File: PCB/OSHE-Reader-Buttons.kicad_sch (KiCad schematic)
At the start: 10 parts, among them SW1 SW_Push, SW2 SW_Push, SW3 SW_Push, SW4 SW_Push, SW5 SW_Push

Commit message: Footprint assignments
Added more footprints
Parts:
- R14, R15, R16, R17, R18: footprint (none) -> Resistor_SMD:R_1206_3216Metric
- SW1, SW2, SW3, SW4, SW5: footprint (none) -> Button_Switch_SMD:SW_Tactile_SPST_NO_Straight_CK_PTS636Sx25SMTRLFS
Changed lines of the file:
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@@
 			)
 		)
-		(property "Footprint" ""
+		(property "Footprint" "Button_Switch_SMD:SW_Tactile_SPST_NO_Straight_CK_PTS636Sx25SMTRLFS"
 			(at 105.41 88.9 0)
 			(effects
@@
 			)
 		)
-		(property "Footprint" ""
+		(property "Footprint" "Button_Switch_SMD:SW_Tactile_SPST_NO_Straight_CK_PTS636Sx25SMTRLFS"
 			(at 54.61 41.91 0)
 			(effects
@@
 			)
 		)
-		(property "Footprint" ""
+		(property "Footprint" "Resistor_SMD:R_1206_3216Metric"
 			(at 111.252 101.6 90)
 			(effects
@@
 			)
 		)
-		(property "Footprint" ""
+		(property "Footprint" "Resistor_SMD:R_1206_3216Metric"
 			(at 137.922 81.28 90)
 			(effects
@@
 			)
 		)
-		(property "Footprint" ""
+		(property "Footprint" "Button_Switch_SMD:SW_Tactile_SPST_NO_Straight_CK_PTS636Sx25SMTRLFS"
 			(at 129.54 68.58 0)
 			(effects
@@
 			)
 		)
-		(property "Footprint" ""
+		(property "Footprint" "Resistor_SMD:R_1206_3216Metric"
 			(at 64.262 82.55 90)
 			(effects
@@
 			)
 		)
-		(property "Footprint" ""
+		(property "Footprint" "Resistor_SMD:R_1206_3216Metric"
 			(at 64.262 52.07 90)
 			(effects
@@
 			)
 		)
-		(property "Footprint" ""
+		(property "Footprint" "Button_Switch_SMD:SW_Tactile_SPST_NO_Straight_CK_PTS636Sx25SMTRLFS"
 			(at 54.61 68.58 0)
 			(effects
@@
 			)
 		)
-		(property "Footprint" ""
+		(property "Footprint" "Button_Switch_SMD:SW_Tactile_SPST_NO_Straight_CK_PTS636Sx25SMTRLFS"
 			(at 128.27 44.45 0)
 			(effects
@@
 			)
 		)
-		(property "Footprint" ""
+		(property "Footprint" "Resistor_SMD:R_1206_3216Metric"
 			(at 139.192 55.88 90)
 			(effects

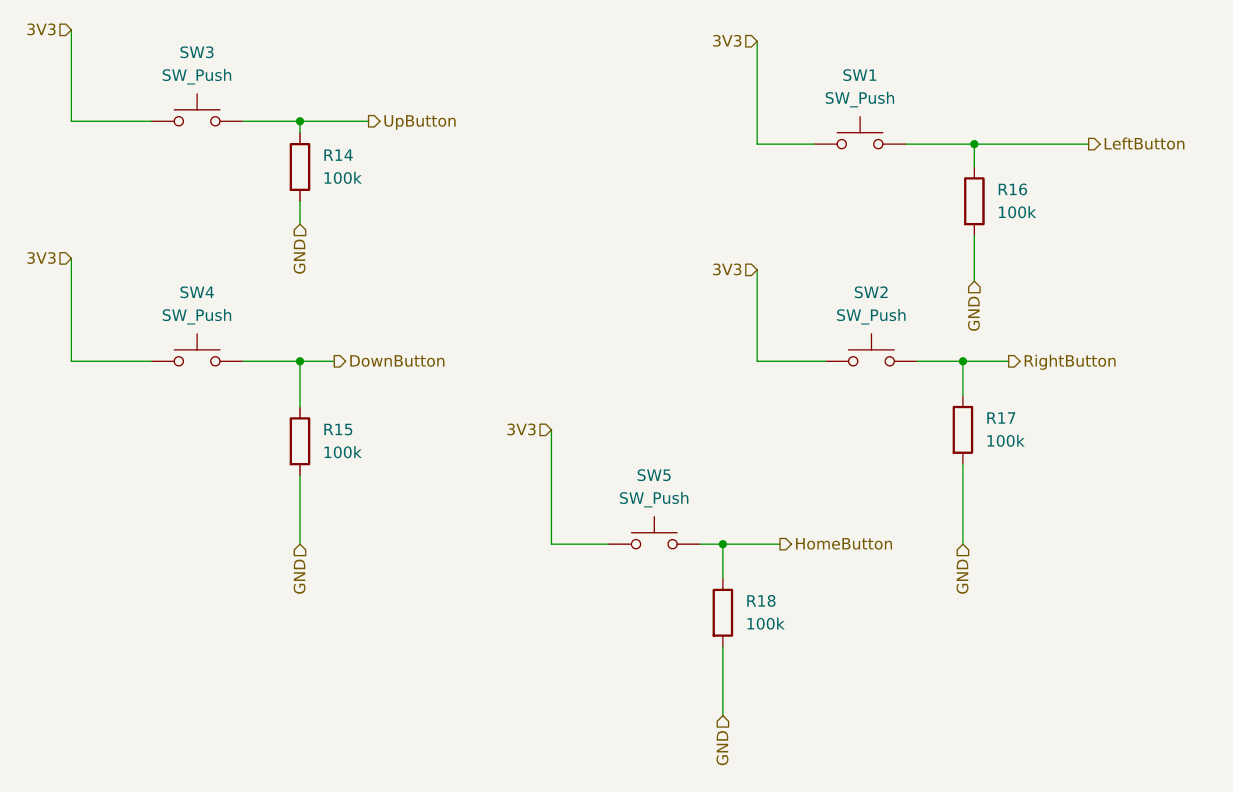
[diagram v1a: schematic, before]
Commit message: Footprints added
All footprints added (problem with J1 for some reason) ((pads of the display driver))
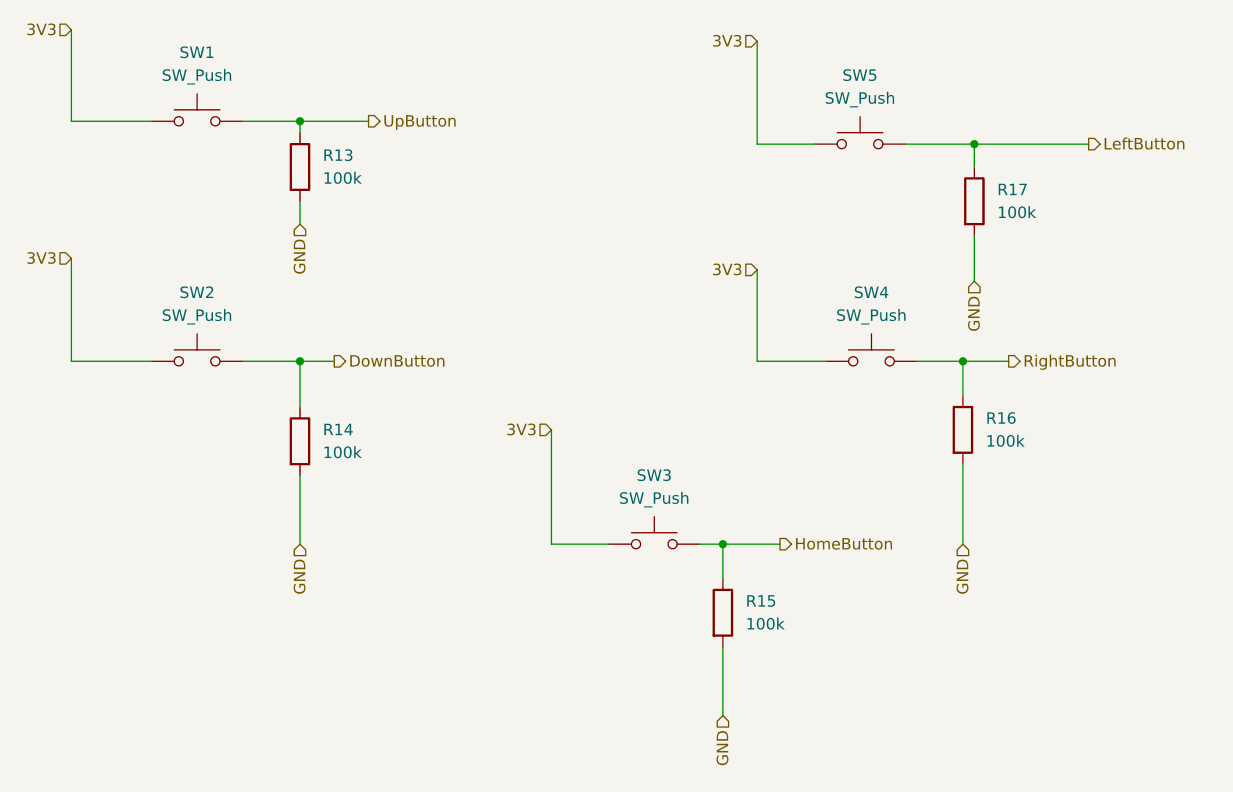
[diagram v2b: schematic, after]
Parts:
- renumbered R14 to R13, R15 to R14, R18 to R15, R17 to R16, R16 to R17, SW3 to SW1, SW4 to SW2, SW5 to SW3, SW2 to SW4, SW1 to SW5
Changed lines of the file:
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@@
 		(dnp no)
 		(fields_autoplaced yes)
-		(property "Reference" "SW5"
+		(property "Reference" "SW3"
 			(at 105.41 86.36 0)
 			(effects
@@
 				)
 			)
+			(project "OSHE-Reader-Buttons"
+				(path "/6556eb4f-dcf8-4b99-98b6-5934a7ce5a03"
+					(reference "SW3")
+					(unit 1)
+				)
+			)
 		)
 	)
@@
 		(on_board yes)
 		(dnp no)
-		(property "Reference" "SW3"
+		(property "Reference" "SW1"
 			(at 54.61 39.37 0)
 			(effects
@@
 				)
 			)
+			(project "OSHE-Reader-Buttons"
+				(path "/6556eb4f-dcf8-4b99-98b6-5934a7ce5a03"
+					(reference "SW1")
+					(unit 1)
+				)
+			)
 		)
 	)
@@
 		(dnp no)
 		(fields_autoplaced yes)
-		(property "Reference" "R18"
+		(property "Reference" "R15"
 			(at 115.57 100.3299 0)
 			(effects
@@
 				)
 			)
+			(project "OSHE-Reader-Buttons"
+				(path "/6556eb4f-dcf8-4b99-98b6-5934a7ce5a03"
+					(reference "R15")
+					(unit 1)
+				)
+			)
 		)
 	)
@@
 		(dnp no)
 		(fields_autoplaced yes)
-		(property "Reference" "R17"
+		(property "Reference" "R16"
 			(at 142.24 80.0099 0)
 			(effects
@@
 				)
 			)
+			(project "OSHE-Reader-Buttons"
+				(path "/6556eb4f-dcf8-4b99-98b6-5934a7ce5a03"
+					(reference "R16")
+					(unit 1)
+				)
+			)
 		)
 	)
@@
 		(dnp no)
 		(fields_autoplaced yes)
-		(property "Reference" "SW2"
+		(property "Reference" "SW4"
 			(at 129.54 66.04 0)
 			(effects
@@
 				)
 			)
+			(project "OSHE-Reader-Buttons"
+				(path "/6556eb4f-dcf8-4b99-98b6-5934a7ce5a03"
+					(reference "SW4")
+					(unit 1)
+				)
+			)
 		)
 	)
@@
 		(dnp no)
 		(fields_autoplaced yes)
-		(property "Reference" "R15"
+		(property "Reference" "R14"
 			(at 68.58 81.2799 0)
 			(effects
@@
 				)
 			)
+			(project "OSHE-Reader-Buttons"
+				(path "/6556eb4f-dcf8-4b99-98b6-5934a7ce5a03"
+					(reference "R14")
+					(unit 1)
+				)
+			)
 		)
 	)
@@
 		(dnp no)
 		(fields_autoplaced yes)
-		(property "Reference" "R14"
+		(property "Reference" "R13"
 			(at 68.58 50.7999 0)
 			(effects
@@
 				)
 			)
+			(project "OSHE-Reader-Buttons"
+				(path "/6556eb4f-dcf8-4b99-98b6-5934a7ce5a03"
+					(reference "R13")
+					(unit 1)
+				)
+			)
 		)
 	)
@@
 		(dnp no)
 		(fields_autoplaced yes)
-		(property "Reference" "SW4"
+		(property "Reference" "SW2"
 			(at 54.61 66.04 0)
 			(effects
@@
 				)
 			)
+			(project "OSHE-Reader-Buttons"
+				(path "/6556eb4f-dcf8-4b99-98b6-5934a7ce5a03"
+					(reference "SW2")
+					(unit 1)
+				)
+			)
 		)
 	)
@@
 		(dnp no)
 		(fields_autoplaced yes)
-		(property "Reference" "SW1"
+		(property "Reference" "SW5"
 			(at 128.27 41.91 0)
 			(effects
@@
 				)
 			)
+			(project "OSHE-Reader-Buttons"
+				(path "/6556eb4f-dcf8-4b99-98b6-5934a7ce5a03"
+					(reference "SW5")
+					(unit 1)
+				)
+			)
 		)
 	)
@@
 		(dnp no)
 		(fields_autoplaced yes)
-		(property "Reference" "R16"
+		(property "Reference" "R17"
 			(at 143.51 54.6099 0)
 			(effects
@@
 				)
 			)
-		)
-	)
+			(project "OSHE-Reader-Buttons"
+				(path "/6556eb4f-dcf8-4b99-98b6-5934a7ce5a03"
+					(reference "R17")
+					(unit 1)
+				)
+			)
+		)
+	)
+	(sheet_instances
+		(path "/"
+			(page "1")
+		)
+	)
+	(embedded_fonts no)
 )

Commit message: Did a bunch of work with final preparations of the schematic for pcb routing
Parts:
- renumbered R13 to R14, R14 to R15, R17 to R16, R16 to R17, R15 to R18, SW5 to SW1, SW4 to SW2, SW1 to SW3, SW2 to SW4, SW3 to SW5
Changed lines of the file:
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@@
 		(dnp no)
 		(fields_autoplaced yes)
-		(property "Reference" "SW3"
+		(property "Reference" "SW5"
 			(at 105.41 86.36 0)
 			(effects
@@
 		(on_board yes)
 		(dnp no)
-		(property "Reference" "SW1"
+		(property "Reference" "SW3"
 			(at 54.61 39.37 0)
 			(effects
@@
 		(dnp no)
 		(fields_autoplaced yes)
-		(property "Reference" "R15"
+		(property "Reference" "R18"
 			(at 115.57 100.3299 0)
 			(effects
@@
 		(dnp no)
 		(fields_autoplaced yes)
-		(property "Reference" "R16"
+		(property "Reference" "R17"
 			(at 142.24 80.0099 0)
 			(effects
@@
 		(dnp no)
 		(fields_autoplaced yes)
-		(property "Reference" "SW4"
+		(property "Reference" "SW2"
 			(at 129.54 66.04 0)
 			(effects
@@
 		(dnp no)
 		(fields_autoplaced yes)
-		(property "Reference" "R14"
+		(property "Reference" "R15"
 			(at 68.58 81.2799 0)
 			(effects
@@
 		(dnp no)
 		(fields_autoplaced yes)
-		(property "Reference" "R13"
+		(property "Reference" "R14"
 			(at 68.58 50.7999 0)
 			(effects
@@
 		(dnp no)
 		(fields_autoplaced yes)
-		(property "Reference" "SW2"
+		(property "Reference" "SW4"
 			(at 54.61 66.04 0)
 			(effects
@@
 		(dnp no)
 		(fields_autoplaced yes)
-		(property "Reference" "SW5"
+		(property "Reference" "SW1"
 			(at 128.27 41.91 0)
 			(effects
@@
 		(dnp no)
 		(fields_autoplaced yes)
-		(property "Reference" "R17"
+		(property "Reference" "R16"
 			(at 143.51 54.6099 0)
 			(effects

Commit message: Started routing PCB & added case dxf for reference
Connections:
- net 3V3: now also SW1.2; no longer SW1.1
- net LeftButton: now also SW1.1; no longer SW1.2
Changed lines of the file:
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@@
 		(lib_id "Switch:SW_Push")
 		(at 128.27 49.53 0)
+		(mirror y)
 		(unit 1)
 		(exclude_from_sim no)
@@
 		(on_board yes)
 		(dnp no)
-		(fields_autoplaced yes)
 		(property "Reference" "SW1"
 			(at 128.27 41.91 0)
